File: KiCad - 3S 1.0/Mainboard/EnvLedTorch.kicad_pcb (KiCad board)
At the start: 2 copper layers, 24.8 x 65 mm, 49 parts, among them J1 USB_C_Receptacle_USB2.0, J101 Conn_01x02, Q1 BSP89, Q2 BSP89, Q3 BSP89, Q4 AO3401A, Q5 AO3401A, U1 HY2213, U2 HY2213, U3 HY2213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

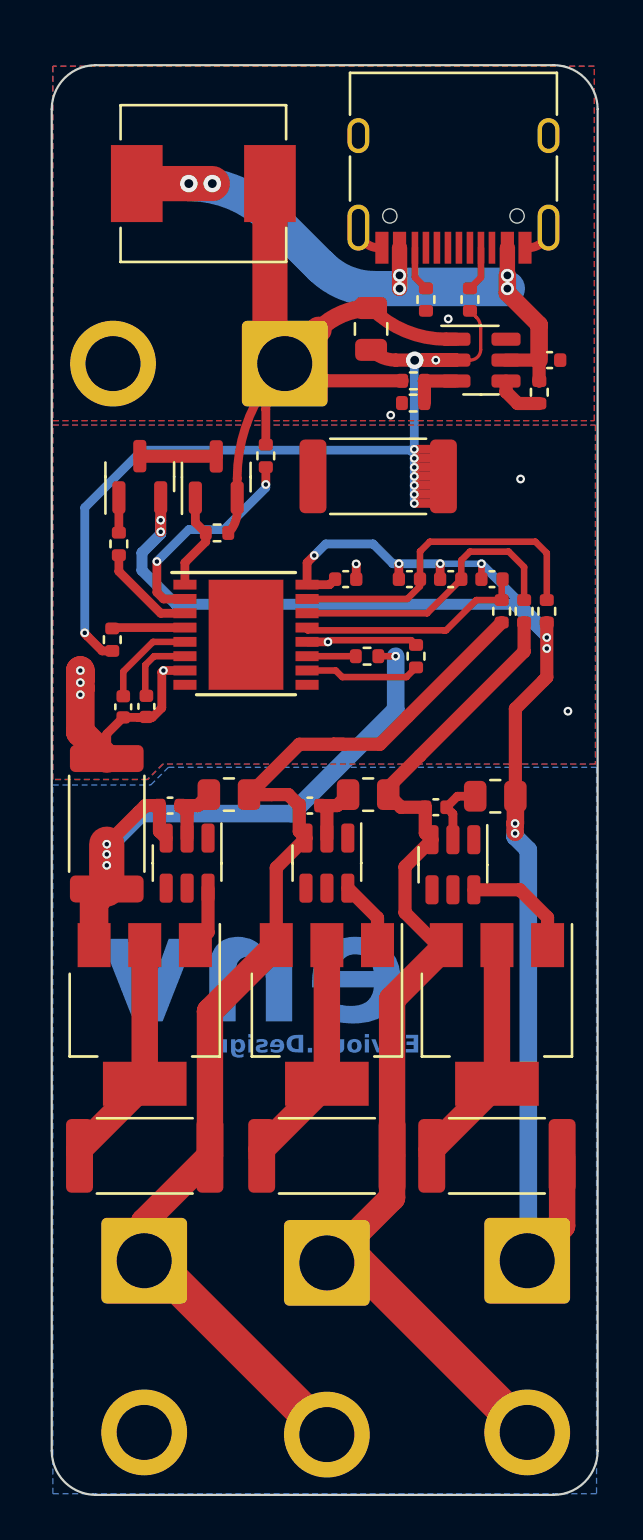
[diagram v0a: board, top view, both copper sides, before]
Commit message: Finished up LED PCB and made some small tweaks and fixes to main board.
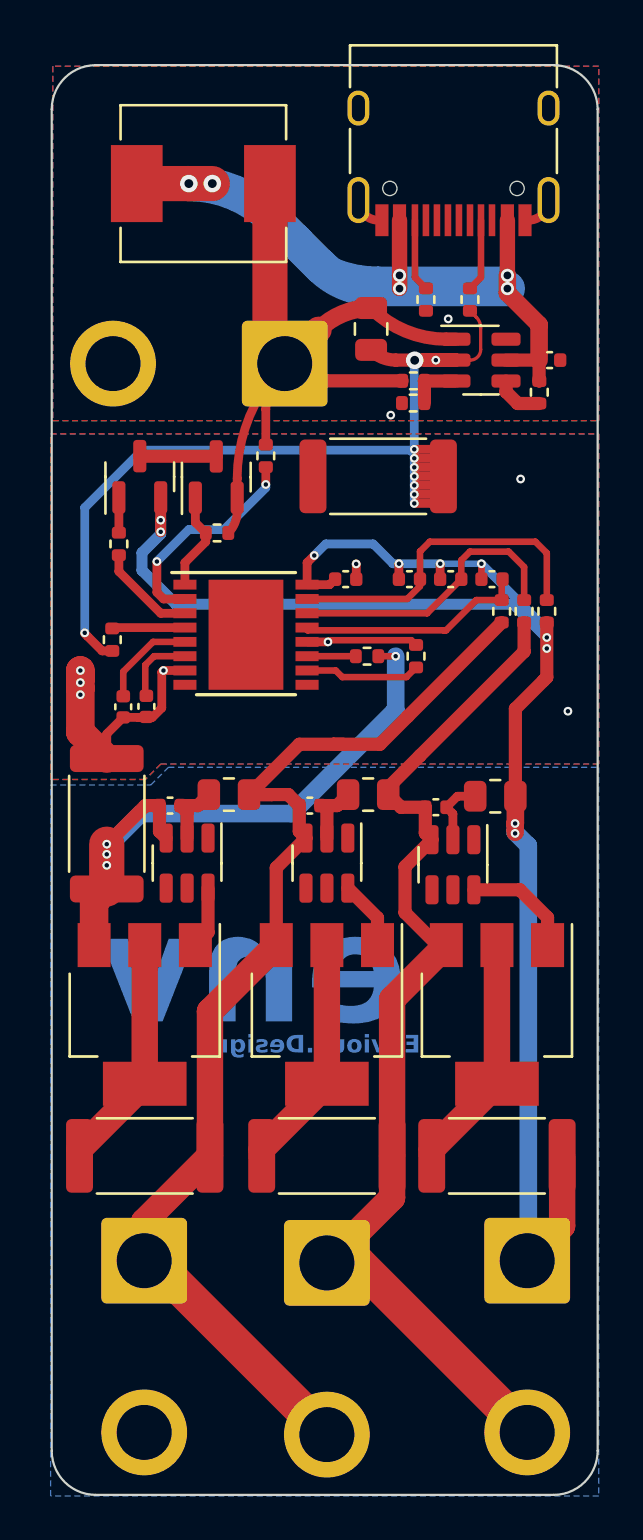
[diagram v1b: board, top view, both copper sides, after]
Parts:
- moved J1 1.25 mm to (36.0, 21.8)
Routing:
- net VBUS: track 39.9 -> 52.4 mm
- net Net-(J1-CC2): track 2.05 -> 3.30 mm
- net Net-(J1-CC1): track 2.05 -> 3.30 mm
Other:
- rule pad_to_mask_clearance: 0.051 -> 0.005
- rule solder_mask_min_width: 0.09 -> 0.005
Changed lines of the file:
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@@
       (dielectric_constraints no)
     )
-    (pad_to_mask_clearance 0.051)
-    (solder_mask_min_width 0.09)
+    (pad_to_mask_clearance 0.005)
+    (solder_mask_min_width 0.005)
     (pcbplotparams
       (layerselection 0x00310fc_ffffffff)
@@
   )
   (footprint "Connector_USB:USB_C_Receptacle_HRO_TYPE-C-31-M-12" (layer "F.Cu")
-    (at 36 23 180)
+    (at 36 21.75 180)
     (descr "USB Type-C receptacle for USB 2.0 and PD, http://www.krhro.com/uploads/soft/180320/1-1P320120243.pdf")
     (tags "usb usb-c 2.0 pd")
@@
   (segment (start 35.2 32.15) (end 35.22 32.13) (width 0.6) (layer "F.Cu") (net 2))
   (segment (start 20.04 45.36) (end 19.37 44.69) (width 0.4) (layer "F.Cu") (net 2))
+  (segment (start 32.75 25.795) (end 32.595 25.795) (width 0.4) (layer "F.Cu") (net 2))
   (segment (start 36.1125 32.15) (end 34.2456 32.15) (width 0.6) (layer "F.Cu") (net 2))
   (segment (start 37.2364 30.6832) (end 37.2364 31.670114) (width 0.15) (layer "F.Cu") (net 2))
+  (segment (start 39.25 25.795) (end 39.405 25.795) (width 0.4) (layer "F.Cu") (net 2))
   (segment (start 35.5425 37.02) (end 35.5425 37.43) (width 0.4) (layer "F.Cu") (net 2))
   (segment (start 35.5425 38.25) (end 35.5425 37.43) (width 0.4) (layer "F.Cu") (net 2))
@@
   (segment (start 34.22 38.25) (end 35.5425 38.25) (width 0.4) (layer "F.Cu") (net 2))
   (segment (start 34.22 37.43) (end 35.5425 37.43) (width 0.4) (layer "F.Cu") (net 2))
-  (segment (start 32.75 27.045) (end 32.595 27.045) (width 0.4) (layer "F.Cu") (net 2))
   (segment (start 35.5425 38.66) (end 35.5425 37.43) (width 0.4) (layer "F.Cu") (net 2))
   (segment (start 19.37 44.69) (end 19.25 44.57) (width 0.4) (layer "F.Cu") (net 2))
@@
   (segment (start 35.18 32.13) (end 35.2 32.15) (width 0.6) (layer "F.Cu") (net 2))
   (segment (start 34.2328 32.15) (end 33.383023 32.15) (width 0.6) (layer "F.Cu") (net 2))
-  (segment (start 39.25 27.045) (end 39.405 27.045) (width 0.4) (layer "F.Cu") (net 2))
   (via (at 35.7632 30.2768) (size 0.4) (drill 0.2) (layers "F.Cu" "B.Cu") (free) (net 2))
   (via (at 34.22 36.2) (size 0.4) (drill 0.2) (layers "F.Cu" "B.Cu") (free) (net 2))
@@
   (via (at 34.22 37.43) (size 0.4) (drill 0.2) (layers "F.Cu" "B.Cu") (free) (net 2))
   (via (at 34.22 38.66) (size 0.4) (drill 0.2) (layers "F.Cu" "B.Cu") (free) (net 2))
-  (arc (start 39.405 27.045) (mid 40.052003 26.777003) (end 40.32 26.13) (width 0.4) (layer "F.Cu") (net 2))
   (arc (start 33.383023 32.15) (mid 32.774165 32.02889) (end 32.258 31.684) (width 0.6) (layer "F.Cu") (net 2))
   (arc (start 37.033601 30.193601) (mid 37.183694 30.418231) (end 37.2364 30.6832) (width 0.15) (layer "F.Cu") (net 2))
+  (arc (start 32.595 25.795) (mid 31.947997 25.527003) (end 31.68 24.88) (width 0.4) (layer "F.Cu") (net 2))
   (arc (start 37.2364 31.670114) (mid 37.095845 32.009445) (end 36.756514 32.15) (width 0.15) (layer "F.Cu") (net 2))
-  (arc (start 32.595 27.045) (mid 31.947997 26.777003) (end 31.68 26.13) (width 0.4) (layer "F.Cu") (net 2))
+  (arc (start 39.405 25.795) (mid 40.052003 25.527003) (end 40.32 24.88) (width 0.4) (layer "F.Cu") (net 2))
   (segment (start 19.25 44.54) (end 19.25 38.85) (width 0.4) (layer "B.Cu") (net 2))
   (segment (start 34.22 32.15) (end 35.2 32.15) (width 0.4) (layer "B.Cu") (net 2))
@@
   (segment (start 33.55 28.3) (end 33.55 28.9) (width 0.7) (layer "F.Cu") (net 4))
   (segment (start 21.613 24.13) (end 23.9268 24.13) (width 1.6) (layer "F.Cu") (net 4))
-  (segment (start 38.45 28.3) (end 38.45 27.045) (width 0.7) (layer "F.Cu") (net 4))
   (segment (start 23.9268 24.13) (end 23.9776 24.13) (width 1.6) (layer "F.Cu") (net 4))
-  (segment (start 33.55 27.045) (end 33.55 28.3) (width 0.7) (layer "F.Cu") (net 4))
   (segment (start 39.89 32.15) (end 39.89 33.09) (width 0.6) (layer "F.Cu") (net 4))
   (segment (start 39.89 32.15) (end 38.3875 32.15) (width 0.6) (layer "F.Cu") (net 4))
   (segment (start 38.45 29.1) (end 38.45 28.3) (width 0.8) (layer "F.Cu") (net 4))
   (segment (start 39.89 32.15) (end 39.89 30.54) (width 0.8) (layer "F.Cu") (net 4))
+  (segment (start 33.55 25.795) (end 33.55 28.3) (width 0.7) (layer "F.Cu") (net 4))
+  (segment (start 38.45 28.3) (end 38.45 25.795) (width 0.7) (layer "F.Cu") (net 4))
   (segment (start 23.9776 24.13) (end 25.0444 24.13) (width 1.6) (layer "F.Cu") (net 4))
   (segment (start 38.45 28.9) (end 38.45 28.3) (width 0.7) (layer "F.Cu") (net 4))
@@
   (via (at 33.55 28.3) (size 0.6) (drill 0.35) (layers "F.Cu" "B.Cu") (net 4))
   (via (at 25.0444 24.13) (size 0.8) (drill 0.4) (layers "F.Cu" "B.Cu") (net 4))
-  (segment (start 29.972 27.8892) (end 27.793326 25.710526) (width 1.6) (layer "B.Cu") (net 4))
+  (segment (start 29.972 27.8892) (end 28.833937 26.751137) (width 1.6) (layer "B.Cu") (net 4))
   (segment (start 38.45 28.9) (end 33.55 28.9) (width 0.7) (layer "B.Cu") (net 4))
   (segment (start 33.55 28.3) (end 38.45 28.3) (width 0.7) (layer "B.Cu") (net 4))
   (segment (start 38.45 28.9) (end 32.412287 28.9) (width 1.6) (layer "B.Cu") (net 4))
+  (segment (start 28.833937 26.751137) (end 27.793326 25.710526) (width 1.6) (layer "B.Cu") (net 4))
+  (segment (start 38.45 28.3) (end 32.573223 28.3) (width 0.8) (layer "B.Cu") (net 4))
   (arc (start 32.412287 28.9) (mid 31.091614 28.637302) (end 29.972 27.8892) (width 1.6) (layer "B.Cu") (net 4))
   (arc (start 27.793326 25.710526) (mid 26.042656 24.540766) (end 23.9776 24.13) (width 1.6) (layer "B.Cu") (net 4))
+  (arc (start 32.573223 28.3) (mid 30.549536 27.897464) (end 28.833937 26.751137) (width 0.8) (layer "B.Cu") (net 4))
   (segment (start 29.870782 30.772818) (end 28.3348 32.3088) (width 1.2) (layer "F.Cu") (net 5))
   (segment (start 33.67 33.09) (end 30.220783 33.09) (width 0.6) (layer "F.Cu") (net 5))
@@
   (arc (start 32.258 29.784) (mid 30.966047 30.040985) (end 29.870782 30.772818) (width 0.8) (layer "F.Cu") (net 5))
   (arc (start 35.676526 31.2) (mid 33.826434 30.831993) (end 32.258 29.784) (width 0.6) (layer "F.Cu") (net 5))
-  (segment (start 37.25 28.39) (end 37.25 27.045) (width 0.3) (layer "F.Cu") (net 6))
   (segment (start 36.75 28.89) (end 37.25 28.39) (width 0.3) (layer "F.Cu") (net 6))
-  (segment (start 34.25 27.045) (end 34.25 28.39) (width 0.3) (layer "F.Cu") (net 10))
+  (segment (start 37.25 28.39) (end 37.25 25.795) (width 0.3) (layer "F.Cu") (net 6))
+  (segment (start 34.25 25.795) (end 34.25 28.39) (width 0.3) (layer "F.Cu") (net 10))
   (segment (start 34.25 28.39) (end 34.75 28.89) (width 0.3) (layer "F.Cu") (net 10))
   (segment (start 24.85 58.150001) (end 24.275001 58.725) (width 0.6) (layer "F.Cu") (net 14))
@@
   (via (at 35.4 41.4) (size 0.4) (drill 0.2) (layers "F.Cu" "B.Cu") (net 51))
   (via (at 22.7 39.42) (size 0.4) (drill 0.2) (layers "F.Cu" "B.Cu") (net 51))
+  (segment (start 38.8 53.6) (end 38.8 53.2) (width 0.8) (layer "B.Cu") (net 51))
   (segment (start 40.24 44.37) (end 37.27 41.4) (width 0.4) (layer "B.Cu") (net 51))
   (segment (start 40.24 45.25) (end 40.24 44.37) (width 0.4) (layer "B.Cu") (net 51))
@@
   (segment (start 35.4 41.4) (end 33.525 41.4) (width 0.4) (layer "B.Cu") (net 51))
   (segment (start 21.85 41.7) (end 23.39 43.24) (width 0.5) (layer "B.Cu") (net 51))
-  (segment (start 38.8 53.8) (end 39.4 54.4) (width 0.8) (layer "B.Cu") (net 51))
+  (segment (start 38.8 53.6) (end 39.4 54.2) (width 0.8) (layer "B.Cu") (net 51))
   (segment (start 30.2 40.5) (end 32.35 40.5) (width 0.4) (layer "B.Cu") (net 51))
-  (segment (start 39.4 73.0125) (end 39.35 73.0625) (width 0.8) (layer "B.Cu") (net 51))
-  (segment (start 38.8 53.6) (end 38.8 53.8) (width 0.8) (layer "B.Cu") (net 51))
   (segment (start 21.85 40.9) (end 21.85 41.7) (width 0.5) (layer "B.Cu") (net 51))
   (segment (start 22.7 40.05) (end 21.85 40.9) (width 0.5) (layer "B.Cu") (net 51))
+  (segment (start 39.4 73.0125) (end 39.35 73.0625) (width 0.8) (layer "B.Cu") (net 51))
   (segment (start 38.73 43.24) (end 40.24 44.75) (width 0.5) (layer "B.Cu") (net 51))
   (segment (start 22.7 39.42) (end 22.7 40.05) (width 0.5) (layer "B.Cu") (net 51))
   (segment (start 29.675 41.025) (end 30.2 40.5) (width 0.4) (layer "B.Cu") (net 51))
-  (segment (start 39.4 54.4) (end 39.4 73.0125) (width 0.8) (layer "B.Cu") (net 51))
   (segment (start 32.35 40.5) (end 33.25 41.4) (width 0.4) (layer "B.Cu") (net 51))
   (segment (start 37.27 41.4) (end 35.4 41.4) (width 0.3) (layer "B.Cu") (net 51))
   (segment (start 23.39 43.24) (end 38.73 43.24) (width 0.5) (layer "B.Cu") (net 51))
+  (segment (start 39.4 54.2) (end 39.4 73.0125) (width 0.8) (layer "B.Cu") (net 51))
   (segment (start 22.03 48.38) (end 22.05 48.36) (width 0.4) (layer "F.Cu") (net 52))
   (segment (start 21.7 48.38) (end 22.03 48.38) (width 0.4) (layer "F.Cu") (net 52))
@@
     (polygon
       (pts
-        (xy 17.8 35.1)
-        (xy 42.45 35.1)
-        (xy 42.45 50.5)
-        (xy 22.8 50.5)
-        (xy 22.1 51.2)
-        (xy 17.8 51.2)
+        (xy 17.7 35.5)
+        (xy 42.6 35.5)
+        (xy 42.6 50.5)
+        (xy 22.7 50.5)
+        (xy 22 51.2)
+        (xy 17.7 51.2)
       )
     )
@@
       (pts
         (xy 17.8 34.9)
-        (xy 42.4 34.9)
-        (xy 42.4 18.8)
+        (xy 42.6 34.9)
+        (xy 42.6 18.8)
         (xy 17.8 18.8)
       )
@@
     (polygon
       (pts
-        (xy 17.8 51.45)
+        (xy 17.7 51.45)
         (xy 22.25 51.45)
         (xy 23.05 50.65)
-        (xy 42.5 50.65)
-        (xy 42.5 83.65)
-        (xy 17.8 83.65)
+        (xy 42.6 50.65)
+        (xy 42.6 83.75)
+        (xy 17.7 83.75)
       )
     )
